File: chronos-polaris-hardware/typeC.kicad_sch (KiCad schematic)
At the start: 3 parts, among them U4 TYPE-C_14PLC-H10_0

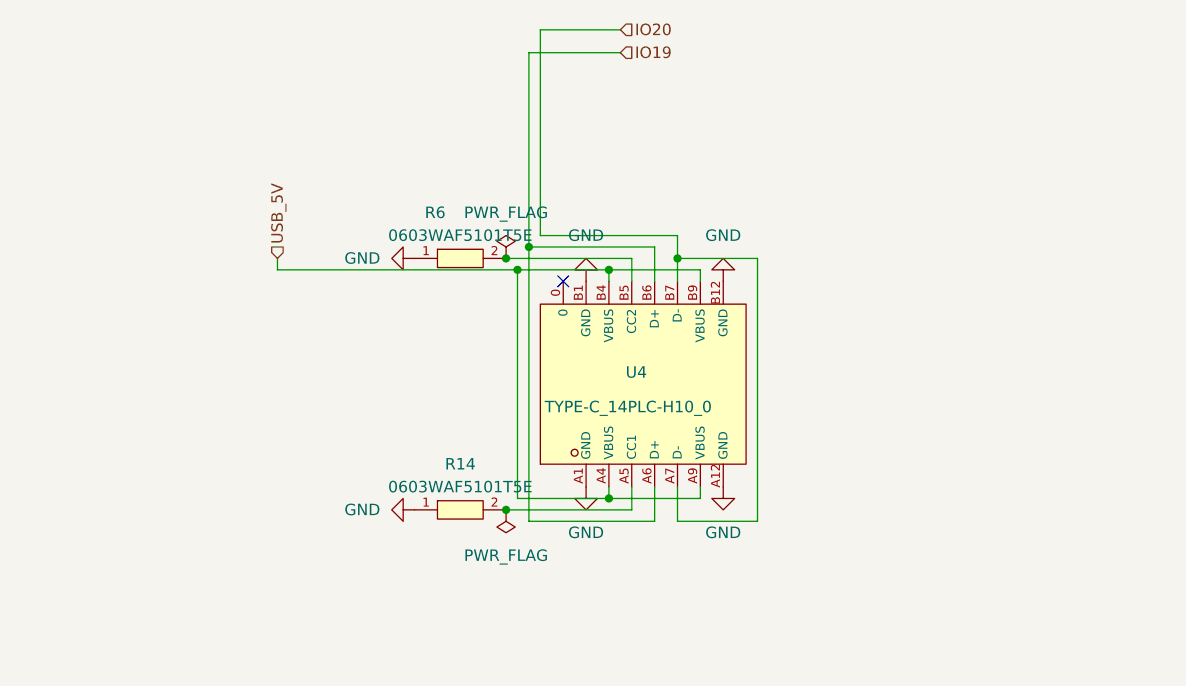
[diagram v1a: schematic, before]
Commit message: Schematic Changes as per DR1 Suggestions
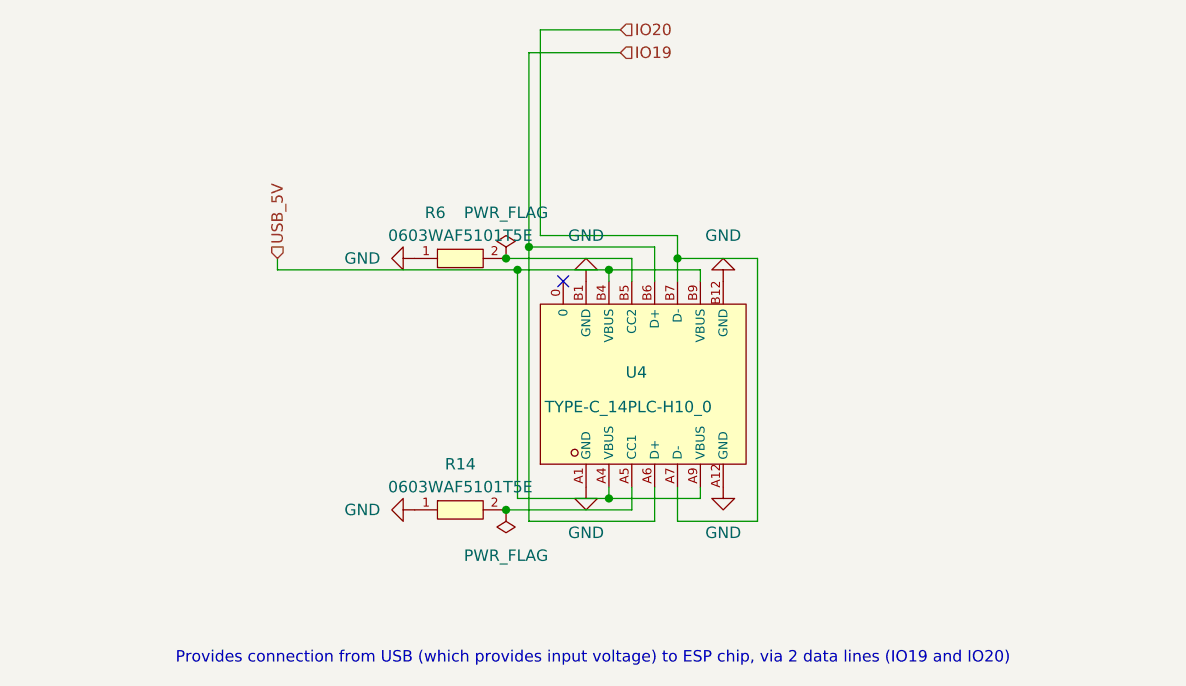
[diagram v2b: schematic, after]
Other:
- note added: "Provides connection from USB (which provides input voltage) to ESP chip, via 2 data lines (IO19 and IO20)"
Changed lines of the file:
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@@
+		)
+	)
+	(text "Provides connection from USB (which provides input voltage) to ESP chip, via 2 data lines (IO19 and IO20)"
+		(exclude_from_sim no)
+		(at 163.322 128.27 0)
+		(effects
+			(font
+				(size 1.27 1.27)
+			)
 		)
 	)
